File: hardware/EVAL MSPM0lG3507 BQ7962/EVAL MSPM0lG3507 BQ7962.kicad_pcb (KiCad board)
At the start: 2 copper layers, 72.5 x 101.3 mm, 156 parts, among them J1 Conn_01x09_Socket, J10 Screw_Terminal_01x02, J11 Screw_Terminal_01x02, J12 Screw_Terminal_01x02, J13 Screw_Terminal_01x02, J14 Screw_Terminal_01x02, J15 Conn_01x02_Pin, J17 Conn_01x02_Pin, J2 Conn_02x05_Odd_Even, J3 Conn_01x04_Pin, J4 Screw_Terminal_01x02, J5 Conn_01x03_Pin, J6 Conn_01x02_Pin, J7 Screw_Terminal_01x02, J8 Screw_Terminal_01x02, J9 Screw_Terminal_01x02, SW1 SW_Push, U10 MCP2542FDxMF, U11 FCX495, U12 FT230XS, U13 PBQ76952PFBT, U14 FCX495, U2 MCU-MSM0G3507SPM, U9 LMR51603XDBVR

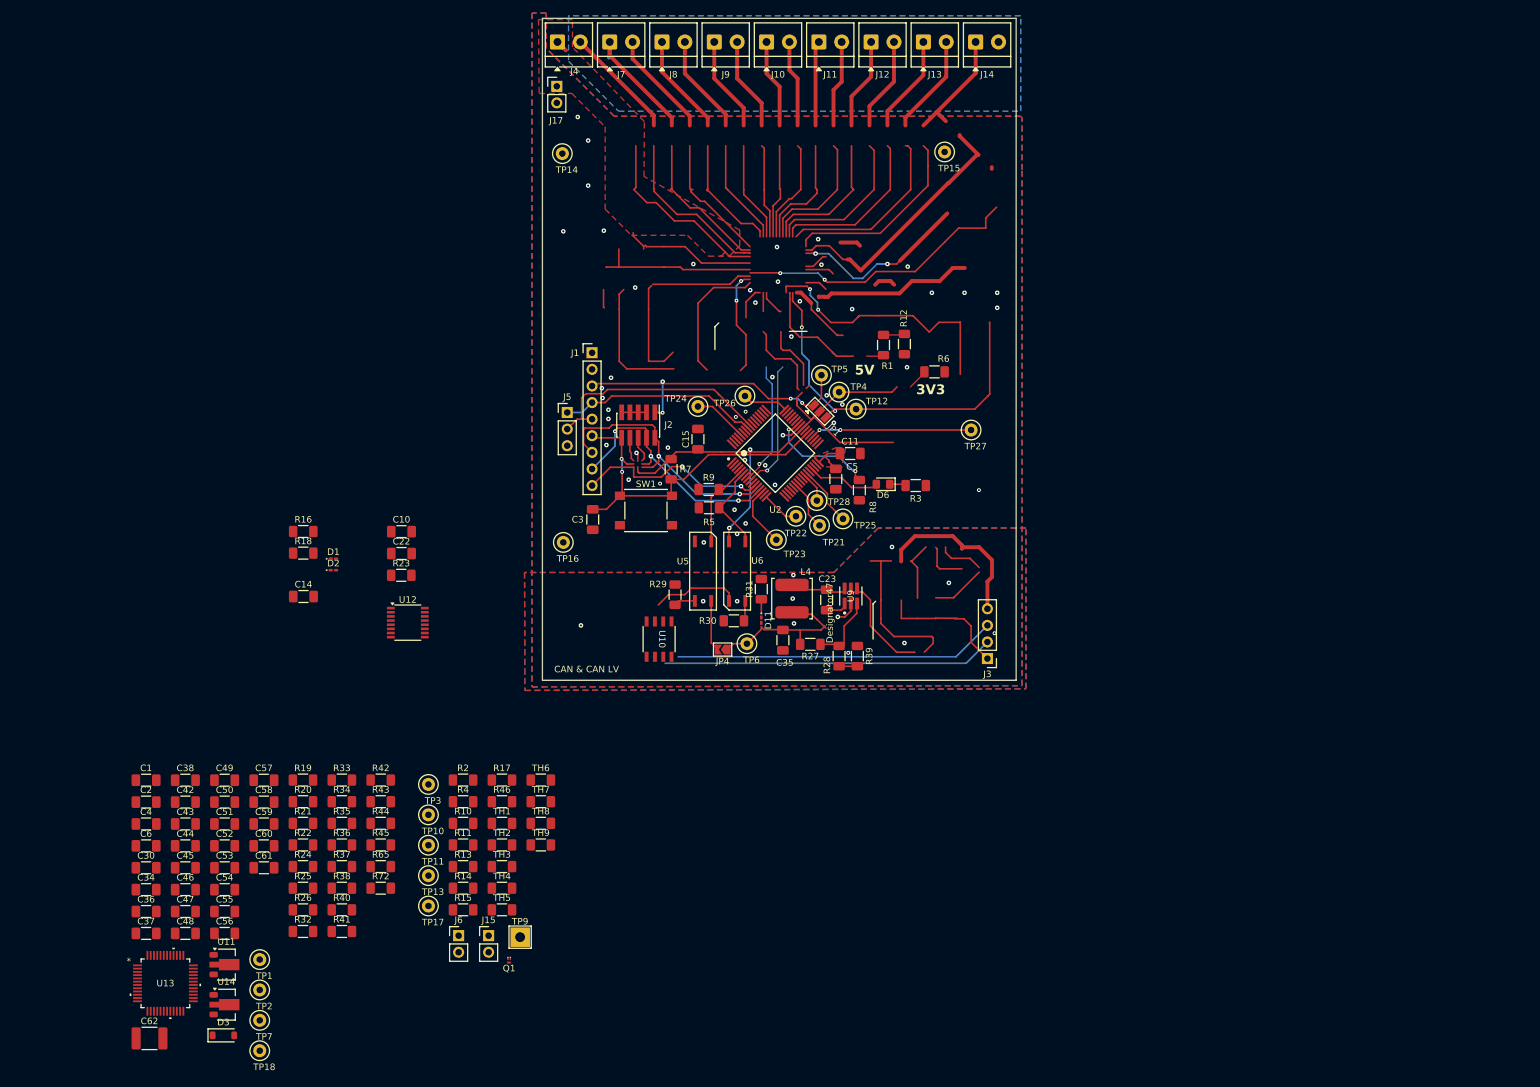
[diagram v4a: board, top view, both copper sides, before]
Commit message: corrected mosfet choice and started jumper board with xds110
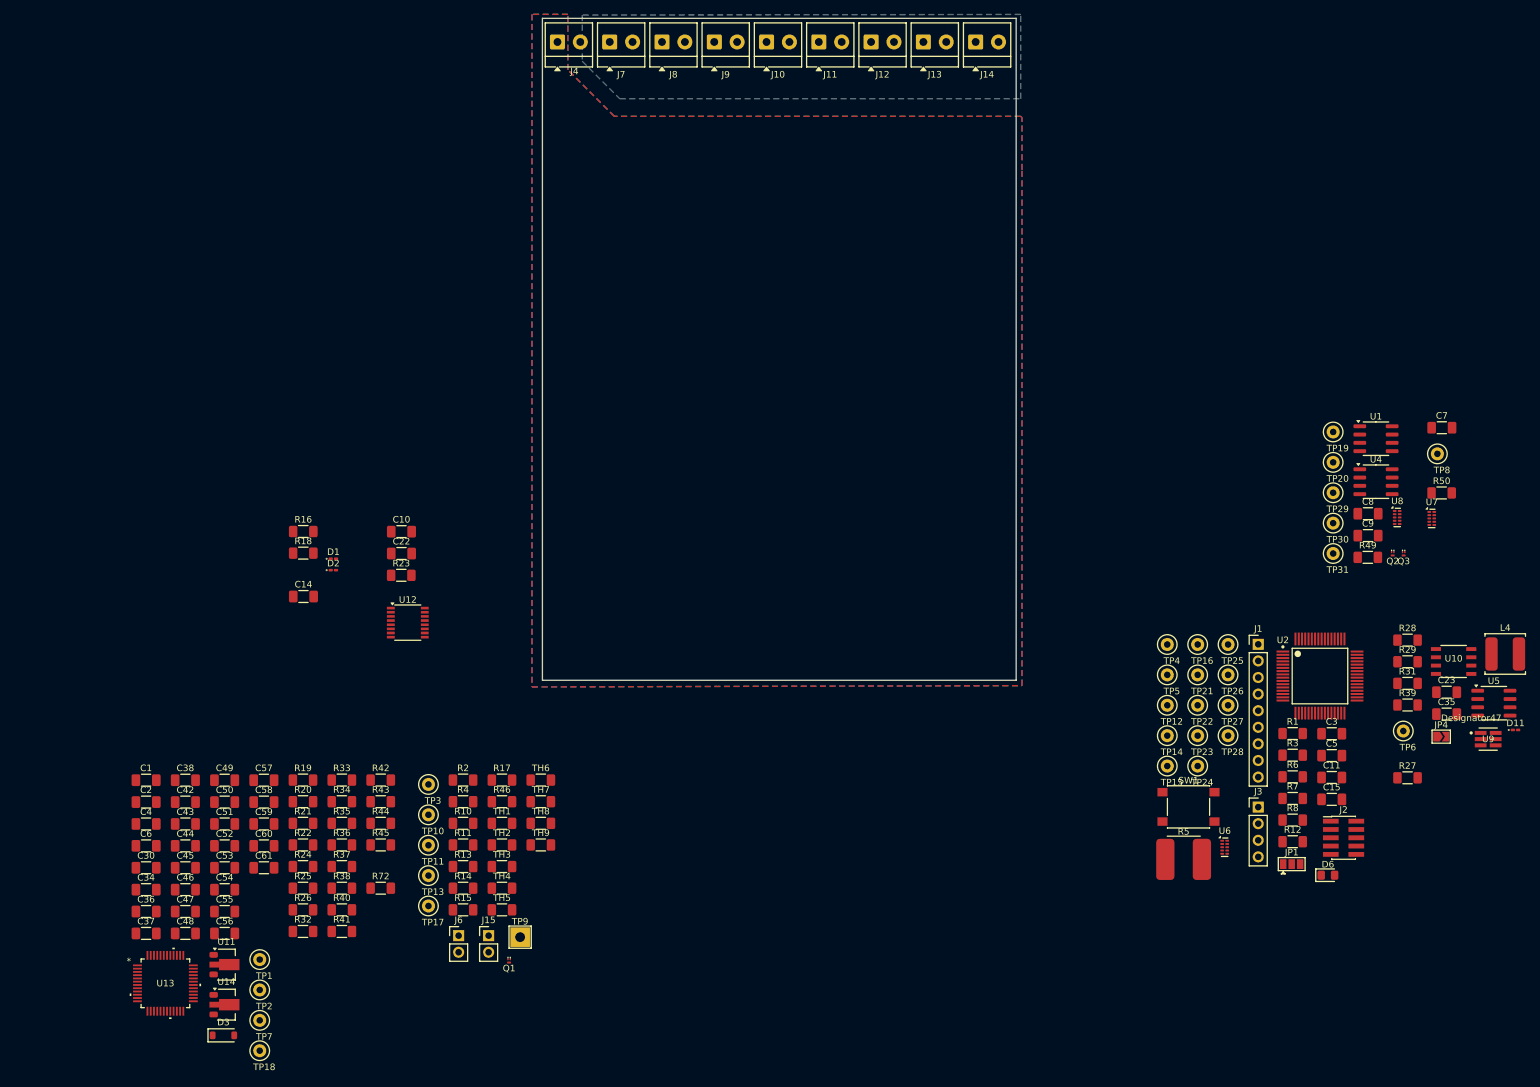
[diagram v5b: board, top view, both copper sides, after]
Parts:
- removed C62: 1u, Capacitor_SMD:C_1812_4532Metric
- removed J17: Conn_01x02_Pin, Connector_PinHeader_2.54mm:PinHeader_1x02_P2.54mm_Vertical
- removed J5: Conn_01x03_Pin, Connector_PinHeader_2.54mm:PinHeader_1x03_P2.54mm_Vertical
- removed R30: 700, Resistor_SMD:R_1206_3216Metric_Pad1.30x1.75mm_HandSolder
- removed R65: 50k, Resistor_SMD:R_1206_3216Metric_Pad1.30x1.75mm_HandSolder
- removed R9: 5k, Resistor_SMD:R_1206_3216Metric_Pad1.30x1.75mm_HandSolder
- added C7: 10u, Capacitor_SMD:C_1206_3216Metric_Pad1.33x1.80mm_HandSolder, F.Cu at (239.8, 86.5)
- added C8: 220n, Capacitor_SMD:C_1206_3216Metric_Pad1.33x1.80mm_HandSolder, F.Cu at (228.5, 99.6)
- added C9: 220n, Capacitor_SMD:C_1206_3216Metric_Pad1.33x1.80mm_HandSolder, F.Cu at (228.5, 103.0)
- added Q2: ~, zzLocalLibraries-Footprints:SOT8001, F.Cu at (232.3, 105.8)
- added Q3: ~, zzLocalLibraries-Footprints:SOT8001, F.Cu at (234.0, 105.8)
- added R49: 4.99k, Resistor_SMD:R_1206_3216Metric_Pad1.30x1.75mm_HandSolder, F.Cu at (228.5, 106.3)
- added R50: 4.99k, Resistor_SMD:R_1206_3216Metric_Pad1.30x1.75mm_HandSolder, F.Cu at (239.8, 96.4)
- added TP19: TestPoint, TestPoint:TestPoint_Loop_D2.50mm_Drill1.0mm_LowProfile, F.Cu at (223.2, 87.1)
- added TP20: TestPoint, TestPoint:TestPoint_Loop_D2.50mm_Drill1.0mm_LowProfile, F.Cu at (223.2, 91.8)
- added TP29: TestPoint, TestPoint:TestPoint_Loop_D2.50mm_Drill1.0mm_LowProfile, F.Cu at (223.2, 96.4)
- added TP30: TestPoint, TestPoint:TestPoint_Loop_D2.50mm_Drill1.0mm_LowProfile, F.Cu at (223.2, 101.0)
- added TP31: TestPoint, TestPoint:TestPoint_Loop_D2.50mm_Drill1.0mm_LowProfile, F.Cu at (223.2, 105.7)
- added TP8: TestPoint, TestPoint:TestPoint_Loop_D2.50mm_Drill1.0mm_LowProfile, F.Cu at (239.2, 90.5)
- added U1: ISO7721D, Package_SO:SOIC-8_3.9x4.9mm_P1.27mm, F.Cu at (229.8, 88.1)
- added U4: ISO7721D, Package_SO:SOIC-8_3.9x4.9mm_P1.27mm, F.Cu at (229.8, 94.7)
- added U7: TPD4E05U06DQA, Package_SON:USON-10_2.5x1.0mm_P0.5mm, F.Cu at (238.3, 100.3)
- added U8: TPD4E05U06DQA, Package_SON:USON-10_2.5x1.0mm_P0.5mm, F.Cu at (233.0, 100.2)
- D3: value D_Zener_Small -> 36V
- R10, R13, R14, R16, R18: value 5k -> 4.99k
- R11, R2, R23, R7: value 50k -> 49.9k
- R15, R46: value 5k -> 100k
- R29: value 700 -> 4.99k
- R5: value 5k -> 1m; footprint Resistor_SMD:R_1206_3216Metric_Pad1.30x1.75mm_HandSolder -> zzLocalLibraries-Footprints:R_shunt_3921
- U5: value ~ -> ISO7721D; footprint zzLocalLibraries-Footprints:ISOM811_SOIC-4_DFG -> Package_SO:SOIC-8_3.9x4.9mm_P1.27mm
- U6: value ~ -> TPD4E05U06DQA; footprint zzLocalLibraries-Footprints:ISOM811_SOIC-4_DFG -> Package_SON:USON-10_2.5x1.0mm_P0.5mm
- moved TP14 128.5 mm to (197.8, 133.6)
- moved J2 125.1 mm to (224.8, 149.2), turned to 0 degrees
- moved U5 122.7 mm to (247.8, 128.6), turned to 0 degrees
- moved U10 121.7 mm to (241.6, 122.3), turned to 0 degrees
- moved C3 117.7 mm to (223.0, 133.3), turned to 0 degrees
- moved D11 116.6 mm to (251.1, 132.7), turned to 0 degrees
- moved R29 112.6 mm to (234.6, 122.3), turned to 0 degrees
- moved C15 111.6 mm to (223.0, 143.3), turned to 0 degrees
- moved J1 111.3 mm to (211.7, 119.6)
- moved JP4 110.8 mm to (239.7, 133.7), turned to 0 degrees
- moved L4 109.5 mm to (249.5, 121.1), turned to 0 degrees
- moved R7 107.6 mm to (217.0, 143.2), turned to 0 degrees
- moved C35 102.2 mm to (240.6, 130.3), turned to 0 degrees
- moved TP6 101.3 mm to (233.9, 132.9)
- moved JP1 100.1 mm to (216.9, 153.2), turned to 0 degrees
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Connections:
- net /GLV CAN TRX/+GLV renamed /GLV CAN TRX/CAN_VDD
- C1 pad 1: Net-(U13-BAT) -> /BQ76952 16C/BAT
- C10 pad 2: /GLV CAN TRX/-GLV -> /GLV CAN TRX/CAN_VSS
- C2 pad 1: Net-(U13-BAT) -> /BQ76952 16C/BAT
- C22 pad 2: /GLV CAN TRX/-GLV -> /GLV CAN TRX/CAN_VSS
- C35 pad 2: /GLV CAN TRX/-GLV -> /GLV CAN TRX/CAN_VSS
- C4 pad 1: Net-(U13-BAT) -> /BQ76952 16C/BAT
- C56 pad 1: Net-(C56-Pad1) -> Net-(D3-K)
- C58 pad 1: Net-(U13-BAT) -> /BQ76952 16C/BAT
- C59 pad 1: Net-(U13-BAT) -> /BQ76952 16C/BAT
- C6 pad 1: Net-(U13-BAT) -> /BQ76952 16C/BAT
- C60 pad 1: Net-(U13-BAT) -> /BQ76952 16C/BAT
- C61 pad 1: Net-(U13-BAT) -> /BQ76952 16C/BAT
- D3 pad 1: unconnected-(D3-K-Pad1) -> Net-(D3-K)
- D3 pad 2: unconnected-(D3-A-Pad2) -> GND
- J10 pad 1: /BQ76952 16C/8P -> /BQ76952 16C/7P
- J10 pad 2: /BQ76952 16C/9P -> /BQ76952 16C/8P
- J11 pad 1: /BQ76952 16C/10P -> /BQ76952 16C/9P
- J11 pad 2: /BQ76952 16C/11P -> /BQ76952 16C/10P
- J12 pad 1: /BQ76952 16C/12P -> /BQ76952 16C/11P
- J12 pad 2: /BQ76952 16C/13P -> /BQ76952 16C/12P
- J13 pad 1: /BQ76952 16C/14P -> /BQ76952 16C/13P
- J13 pad 2: /BQ76952 16C/15P -> /BQ76952 16C/14P
- J14 pad 1: +BATT -> /BQ76952 16C/15P
- J14 pad 2: unconnected-(J14-Pin_2-Pad2) -> /BQ76952 16C/16P
- J3 pad 1: /GLV CAN TRX/-GLV -> /GLV CAN TRX/CAN_VSS
- J4 pad 1: -BATT -> GND
- J4 pad 2: /BQ76952 16C/1P -> /BQ76952 16C/1N
- J7 pad 1: /BQ76952 16C/2P -> /BQ76952 16C/1P
- J7 pad 2: /BQ76952 16C/3P -> /BQ76952 16C/2P
- J8 pad 1: /BQ76952 16C/4P -> /BQ76952 16C/3P
- J8 pad 2: /BQ76952 16C/5P -> /BQ76952 16C/4P
- J9 pad 1: /BQ76952 16C/6P -> /BQ76952 16C/5P
- J9 pad 2: /BQ76952 16C/7P -> /BQ76952 16C/6P
- Q1 pad 2: /BQ76952 16C/RST_SHUT -> Net-(Q1-S)
- R10 pad 2: /BAT -> /BQ76952 16C/BAT
- R11 pad 2: /BQ76952 16C/RST_SHUT -> Net-(Q1-S)
- R14 pad 1: /BAT -> /BQ76952 16C/BAT
- R15 pad 1: Net-(J6-Pin_2) -> Net-(U9-FB)
- R15 pad 2: /BQ0_3.3v -> Net-(D11-A)
- R25 pad 1: -BATT -> /BQ76952 16C/1N
- R27 pad 1: Net-(U9-FB) -> Net-(R27-Pad1)
- R27 pad 2: Net-(D11-A) -> Net-(R27-Pad2)
- R31 pad 2: /GLV CAN TRX/-GLV -> /GLV CAN TRX/CAN_VSS
- R39 pad 1: /GLV CAN TRX/-GLV -> /GLV CAN TRX/CAN_VSS
- R40 pad 1: +BATT -> /BQ76952 16C/16P
- R44 pad 1: -BATT -> /BQ76952 16C/1N
- R45 pad 1: Net-(R45-Pad1) -> Net-(R27-Pad2)
- R45 pad 2: +BATT -> /BQ76952 16C/16P
- R46 pad 1: Net-(J6-Pin_1) -> Net-(D3-K)
- R46 pad 2: /BQ0_3.3v -> Net-(R27-Pad1)
- R5 pad 2: PA13_CAN_RX -> /BQ76952 16C/1N
- R72 pad 1: Net-(U13-BAT) -> /BQ76952 16C/BAT
- TP18 pad 1: Net-(U13-BAT) -> /BQ76952 16C/BAT
- U11 pad 1: Net-(C56-Pad1) -> Net-(D3-K)
- U11 pad 2: Net-(R45-Pad1) -> Net-(R27-Pad2)
- U11 pad 3: Net-(U13-BAT) -> /BQ76952 16C/BAT
- U12 pad 1: unconnected-(U12-TXD-Pad1) -> Net-(U1-OUTA)
- U12 pad 10: unconnected-(U12-3V3OUT-Pad10) -> Net-(U1-VCC1)
- U12 pad 12: unconnected-(U12-VCC-Pad12) -> /UART_USB/VBUS_5v
- U12 pad 13: unconnected-(U12-GND-Pad13) -> Net-(Q2-S)
- U12 pad 2: unconnected-(U12-~{RTS}-Pad2) -> Net-(U12-~{RTS})
- U12 pad 3: unconnected-(U12-VCCIO-Pad3) -> Net-(U1-VCC1)
- U12 pad 4: unconnected-(U12-RXD-Pad4) -> Net-(U1-INB)
- U12 pad 5: unconnected-(U12-GND-Pad5) -> Net-(Q2-S)
- U12 pad 6: unconnected-(U12-~{CTS}-Pad6) -> Net-(U12-~{CTS})
- U12 pad 8: unconnected-(U12-USBDP-Pad8) -> /UART_USB/D+
- U12 pad 9: unconnected-(U12-USBDM-Pad9) -> /UART_USB/D-
- U13 pad 47: Net-(U13-BAT) -> /BQ76952 16C/BAT
- U2 pad 54: unconnected-(U2-PA8-Pad54) -> PA8_UART0-RTS
- U2 pad 55: unconnected-(U2-PA9-Pad55) -> PA9_UART0-CTS
- U5 pad 1: PA12_CAN_TX -> /GLV CAN TRX/5v
- U5 pad 2: GND -> Net-(U10-TXD)
- U5 pad 3: Net-(U10-TXD) -> Net-(U10-RXD)
- U5 pad 4: /GLV CAN TRX/5v -> /GLV CAN TRX/-GLV
- U6 pad 1: Net-(U10-RXD) -> PA11_UART0-RX_XDS
- U6 pad 2: Net-(U6--TX) -> PA10_UART0-TX_XDS
- U6 pad 3: PA13_CAN_RX -> GND
- U6 pad 4: VDD -> RST_N
- U9 pad 2: /GLV CAN TRX/-GLV -> /GLV CAN TRX/CAN_VSS
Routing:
- net (no net): track 792.7 -> 0.00 mm, vias 8 -> 0
- net VDD: track 82.3 -> 0.00 mm, vias 2 -> 0
- net onboard 3.3v src: track 58.5 -> 0.00 mm, vias 2 -> 0
- net RST_N: track 55.2 -> 0.00 mm, vias 2 -> 0
- net /GLV CAN TRX/CAN_L: track 50.7 -> 0.00 mm
- net /GLV CAN TRX/CAN_H: track 49.3 -> 0.00 mm
- net /XDS_3v_supply: track 47.0 -> 0.00 mm, vias 4 -> 0
- net /GLV CAN TRX/CAN_VDD: track 42.3 -> 0.00 mm
- net PA19_SWDIO: track 41.7 -> 0.00 mm, vias 2 -> 0
- net PA20_SWCLK: track 39.3 -> 0.00 mm, vias 3 -> 0
- net PA10_UART0-TX_XDS: track 36.9 -> 0.00 mm
- net PA11_UART0-RX_XDS: track 30.7 -> 0.00 mm
- net PA18: track 30.0 -> 0.00 mm, vias 2 -> 0
- net Net-(D11-A): track 25.5 -> 0.00 mm
- net Net-(U2-PA29): track 24.8 -> 0.00 mm, vias 2 -> 0
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- removed copper zone on F.Cu, net -BATT
- removed copper zone on B.Cu, net /GLV CAN TRX/-GLV
- removed copper zone on F.Cu, net /GLV CAN TRX/-GLV
- removed copper zone on F.Cu, net Net-(U2-VCORE)
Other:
- board text removed: "3V3"
- board text removed: "5V"
- board text removed: "CAN & CAN LV"
- board text removed: "CAN H"
- board text removed: "CAN L"
- board text removed: "CAN_LV+"
- board text removed: "CAN_LV-"

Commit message: indicated layout so someone else can do it
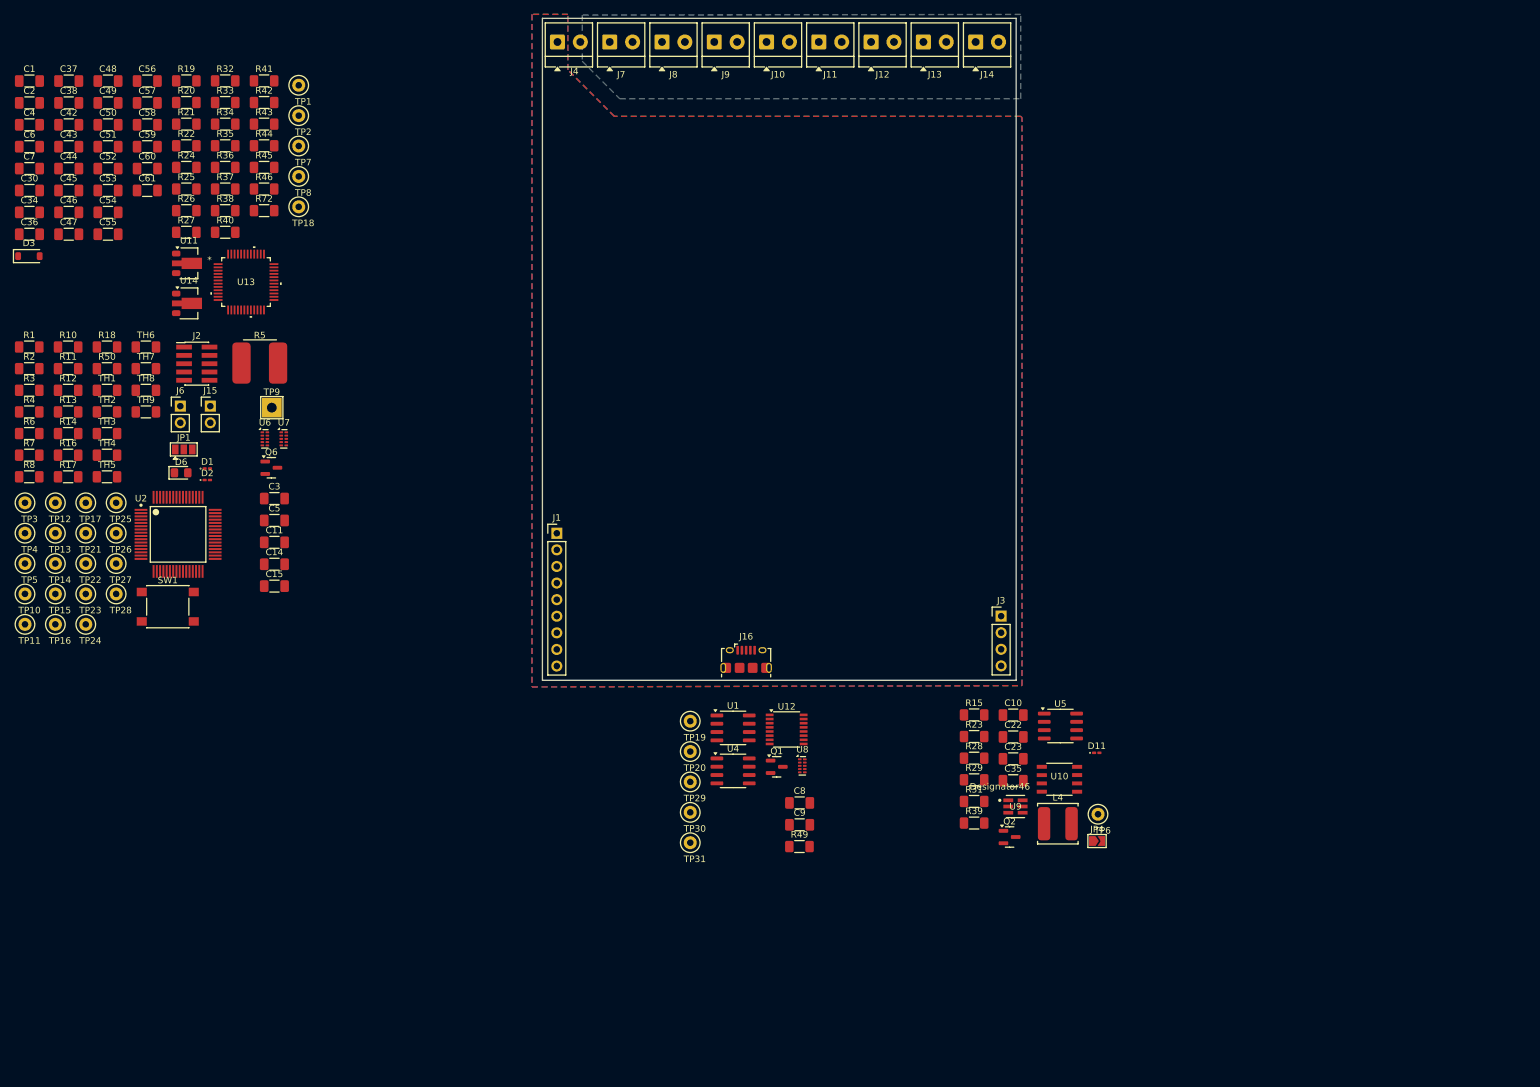
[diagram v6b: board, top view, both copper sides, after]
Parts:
- removed Q3: ~, zzLocalLibraries-Footprints:SOT8001
- added J16: USB_B_Micro, Connector_USB:USB_Micro-B_Amphenol_10118194-0001LF_Horizontal, F.Cu at (133.4, 121.9)
- added Q6: 2N7002, Package_TO_SOT_SMD:SOT-23, F.Cu at (60.7, 92.6)
- Q1, Q2: value ~ -> 2N7002; footprint zzLocalLibraries-Footprints:SOT8001 -> Package_TO_SOT_SMD:SOT-23
- U9: footprint zzLocalLibraries-Footprints:DBV0006A-MFG-IPC_A -> zzLocalLibraries-Footprints:DBV0006A-MFG-IPC_B
- moved C7 219.8 mm to (23.7, 46.8)
- moved R50 205.1 mm to (35.6, 77.4)
- moved R27 204.7 mm to (47.7, 56.5)
- moved R1 202.2 mm to (23.7, 74.1)
- moved R3 201.3 mm to (23.7, 80.7)
- moved R6 200.4 mm to (23.7, 87.3)
- moved R7 200.4 mm to (23.7, 90.7)
- moved R8 200.4 mm to (23.7, 94.0)
- moved R12 199.7 mm to (29.6, 80.7)
- moved J2 189.9 mm to (49.3, 76.7)
- moved D6 186.0 mm to (46.9, 93.3)
- moved JP1 181.0 mm to (47.3, 89.8)
- moved TP8 179.4 mm to (64.9, 48.0)
- moved U7 176.1 mm to (62.6, 88.2)
- moved U2 176.1 mm to (46.4, 102.8)
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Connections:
- C10 pad 2: /GLV CAN TRX/CAN_VSS -> Net-(Q2-S)
- C22 pad 2: /GLV CAN TRX/CAN_VSS -> Net-(Q2-S)
- C35 pad 2: /GLV CAN TRX/CAN_VSS -> Net-(Q2-S)
- C8 pad 2: Net-(Q2-S) -> Net-(Q1-S)
- C9 pad 2: Net-(Q2-S) -> Net-(Q1-S)
- Q1 pad 1: PB26 -> /UART_USB/VBUS_5v
- Q1 pad 3: /BQ0_3.3v -> /UART_USB/GND
- Q2 pad 1: /UART_USB/VBUS_5v -> /GLV CAN TRX/CAN_VDD
- Q2 pad 3: /UART_USB/GND -> /GLV CAN TRX/CAN_VSS
- R11 pad 2: Net-(Q1-S) -> Net-(Q6-S)
- R31 pad 2: /GLV CAN TRX/CAN_VSS -> Net-(Q2-S)
- R39 pad 1: /GLV CAN TRX/CAN_VSS -> Net-(Q2-S)
- R50 pad 2: Net-(Q1-S) -> Net-(Q6-S)
- U1 pad 4: Net-(Q2-S) -> Net-(Q1-S)
- U1 pad 5: Net-(Q3-S) -> GND
- U12 pad 13: Net-(Q2-S) -> Net-(Q1-S)
- U12 pad 5: Net-(Q2-S) -> Net-(Q1-S)
- U4 pad 4: Net-(Q2-S) -> Net-(Q1-S)
- U4 pad 5: Net-(Q3-S) -> GND
- U9 pad 2: /GLV CAN TRX/CAN_VSS -> Net-(Q2-S)
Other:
- board text added: "BQ chip & direct HV stuff"
- board text added: "MSPM0G stuff"
- board text added: "electrically isolated CAN BUS port"
- board text added: "electrically isolated usb connection"
